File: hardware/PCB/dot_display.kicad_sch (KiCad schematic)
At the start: 33 parts, among them U10 MAX7219, U27 MAX7219, U29 MAX7219, U3 MAX7219, U31 MAX7219, U4 MAX7219, U6 MAX7219, U7 MAX7219

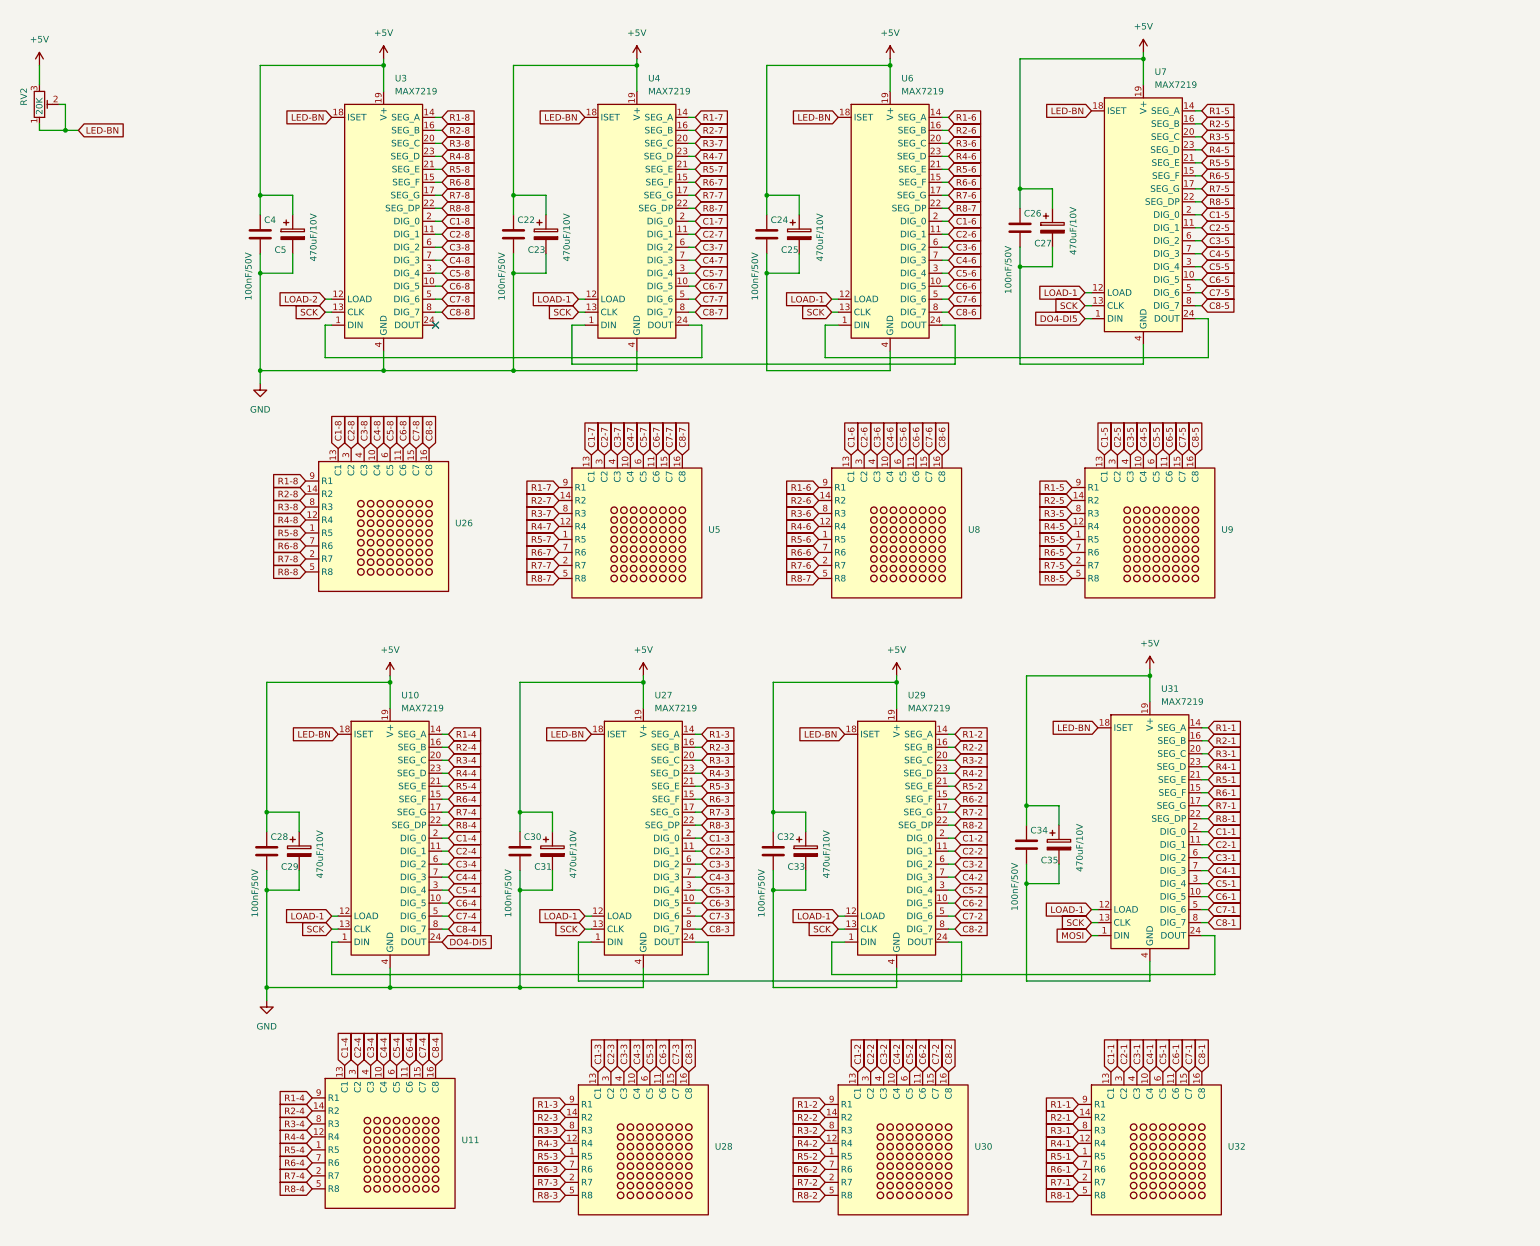
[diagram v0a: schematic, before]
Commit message: added KiCad libraries schematic bugfixes
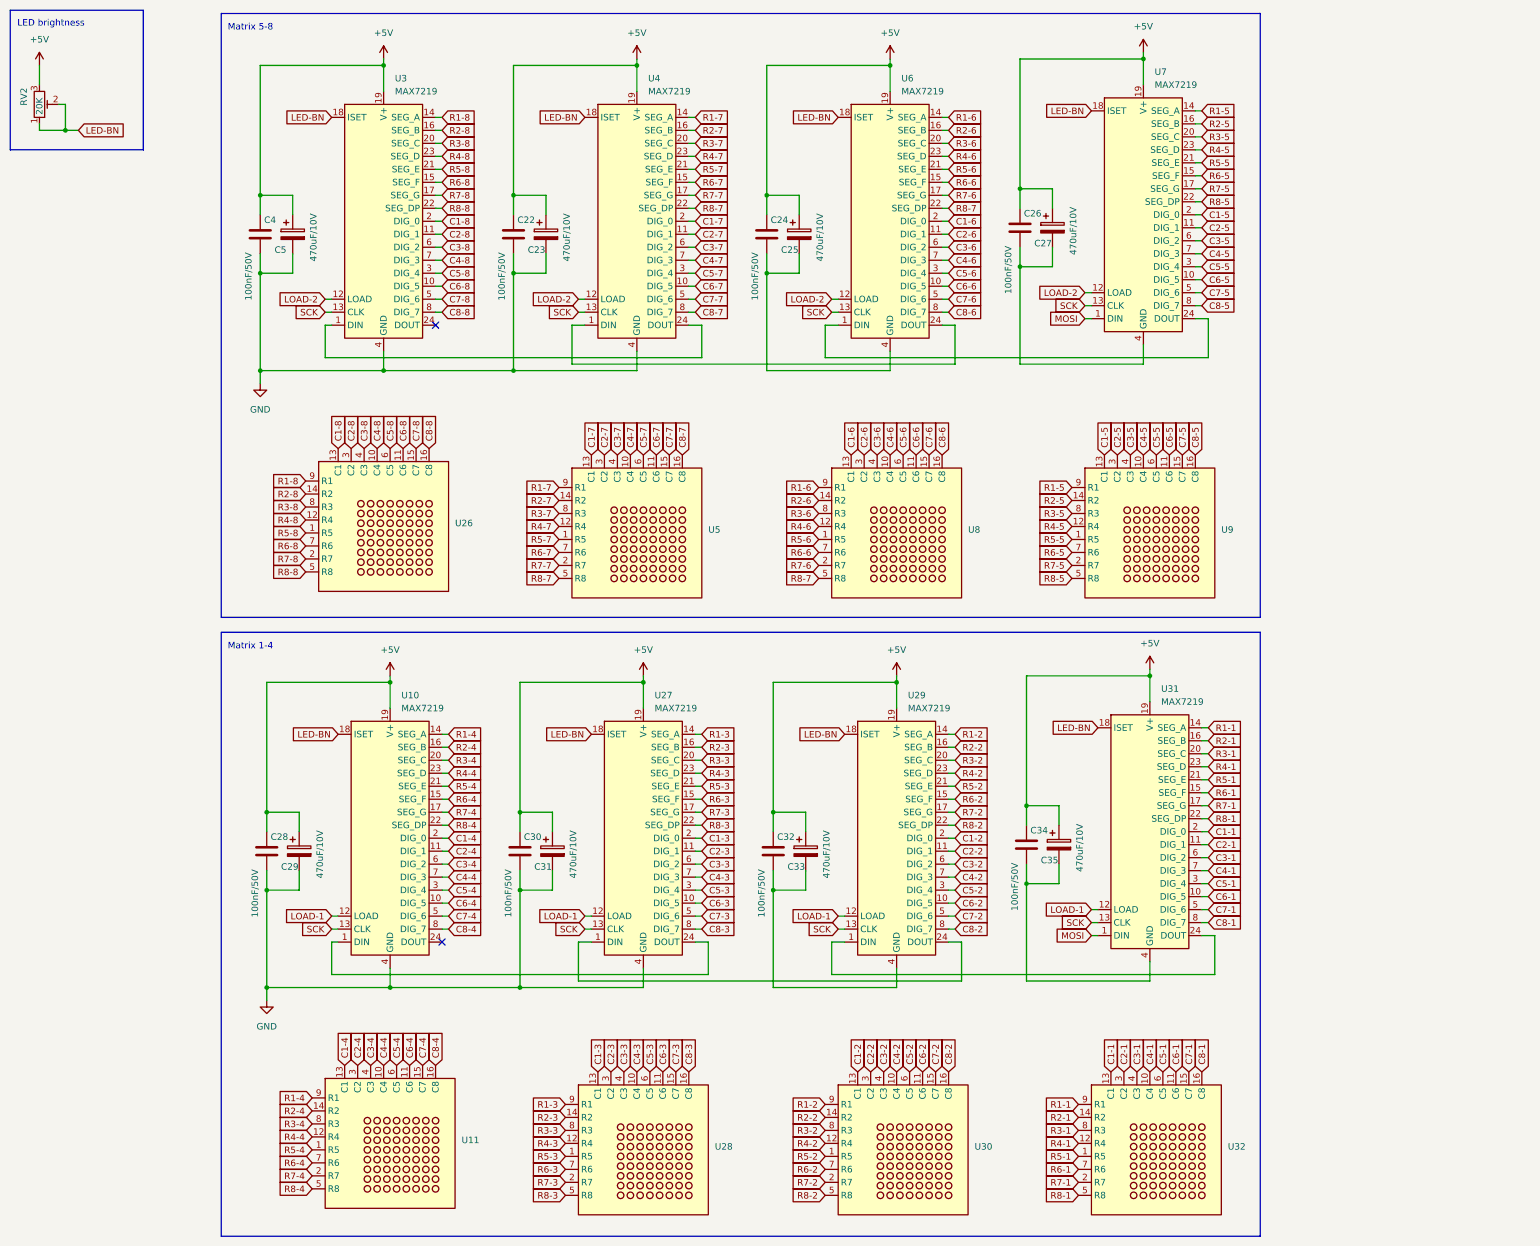
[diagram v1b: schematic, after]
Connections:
- net LOAD-1: no longer U4.12 (LOAD), U6.12 (LOAD), U7.12 (LOAD)
- net LOAD-2: now also U4.12 (LOAD), U6.12 (LOAD), U7.12 (LOAD)
- net MOSI: now also U7.1 (DIN)
- net DO4-DI5: no longer names the net of U10.24 (DOUT)
- net DO4-DI5: no longer U7.1 (DIN)
- no-connect marks 1 -> 2
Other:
- note added: "LED brightness"
- note added: "Matrix 1-4"
- note added: "Matrix 5-8"
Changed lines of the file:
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@@
 	)
 	(no_connect
+		(at 118.11 207.01)
+	)
+	(no_connect
 		(at 116.84 86.36)
 	)
@@
 		)
 	)
+	(rectangle
+		(start 74.93 146.431)
+		(end 278.13 264.541)
+		(stroke
+			(width 0)
+			(type default)
+		)
+		(fill
+			(type none)
+		)
+	)
+	(rectangle
+		(start 74.93 25.4)
+		(end 278.13 143.51)
+		(stroke
+			(width 0)
+			(type default)
+		)
+		(fill
+			(type none)
+		)
+	)
+	(rectangle
+		(start 33.655 24.765)
+		(end 59.69 52.07)
+		(stroke
+			(width 0)
+			(type default)
+		)
+		(fill
+			(type none)
+		)
+	)
+	(text "LED brightness"
+		(exclude_from_sim no)
+		(at 35.052 27.432 0)
+		(effects
+			(font
+				(size 1.27 1.27)
+			)
+			(justify left)
+		)
+	)
+	(text "Matrix 5-8"
+		(exclude_from_sim no)
+		(at 76.2 28.194 0)
+		(effects
+			(font
+				(size 1.27 1.27)
+			)
+			(justify left)
+		)
+	)
+	(text "Matrix 1-4"
+		(exclude_from_sim no)
+		(at 76.2 149.225 0)
+		(effects
+			(font
+				(size 1.27 1.27)
+			)
+			(justify left)
+		)
+	)
 	(global_label "C7-4"
 		(shape input)
@@
 		)
 	)
-	(global_label "DO4-DI5"
+	(global_label "MOSI"
 		(shape input)
 		(at 243.84 85.09 180)
@@
 		)
 		(property "Intersheetrefs" "${INTERSHEET_REFS}"
-			(at 232.3881 85.09 0)
+			(at 236.2586 85.09 0)
 			(effects
 				(font
@@
 		)
 	)
-	(global_label "LOAD-1"
+	(global_label "LOAD-2"
 		(shape input)
 		(at 243.84 80.01 180)
@@
 		)
 	)
-	(global_label "LOAD-1"
+	(global_label "LOAD-2"
 		(shape input)
 		(at 194.31 81.28 180)
@@
 		)
 	)
-	(global_label "LOAD-1"
+	(global_label "LOAD-2"
 		(shape input)
 		(at 144.78 81.28 180)
@@
 				(hide yes)
 			)
-		)
-	)
-	(global_label "DO4-DI5"
-		(shape input)
-		(at 118.11 207.01 0)
-		(fields_autoplaced yes)
-		(effects
-			(font
-				(size 1.27 1.27)
-			)
-			(justify left)
-		)
-		(property "Intersheetrefs" "${INTERSHEET_REFS}"
-			(at 129.5619 207.01 0)
-			(effects
-				(font
-					(size 1.27 1.27)
-				)
-				(justify left)
-				(hide yes)
-			)

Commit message: new harware bugfixes while building the prototype
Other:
- title: Dot Matrix Display -> DigiSlate+
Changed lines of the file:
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@@
 	(paper "A3")
 	(title_block
-		(title "Dot Matrix Display")
-		(date "2024-09-11")
-		(rev "1.0")
+		(title "DigiSlate+")
+		(date "2024-09-05")
+		(rev "1.1")
 	)
 	(junction

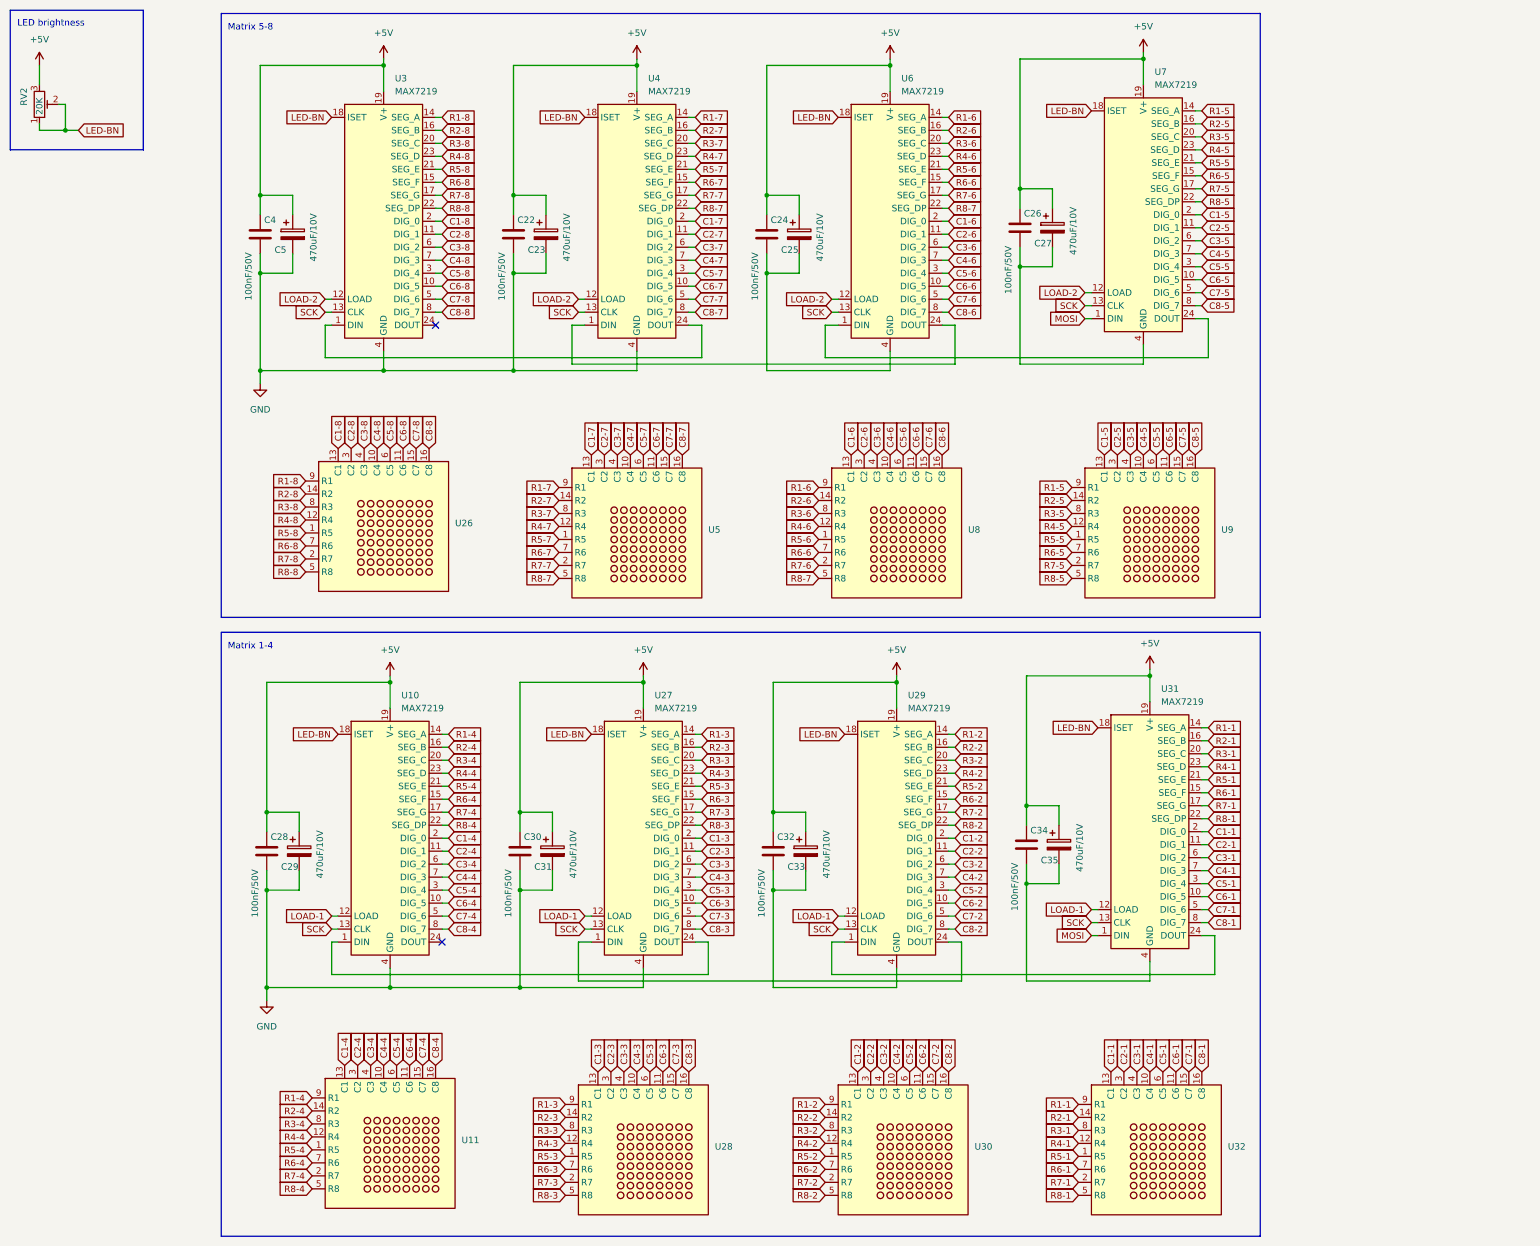
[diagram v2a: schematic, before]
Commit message: level converter added to schematic and pcb
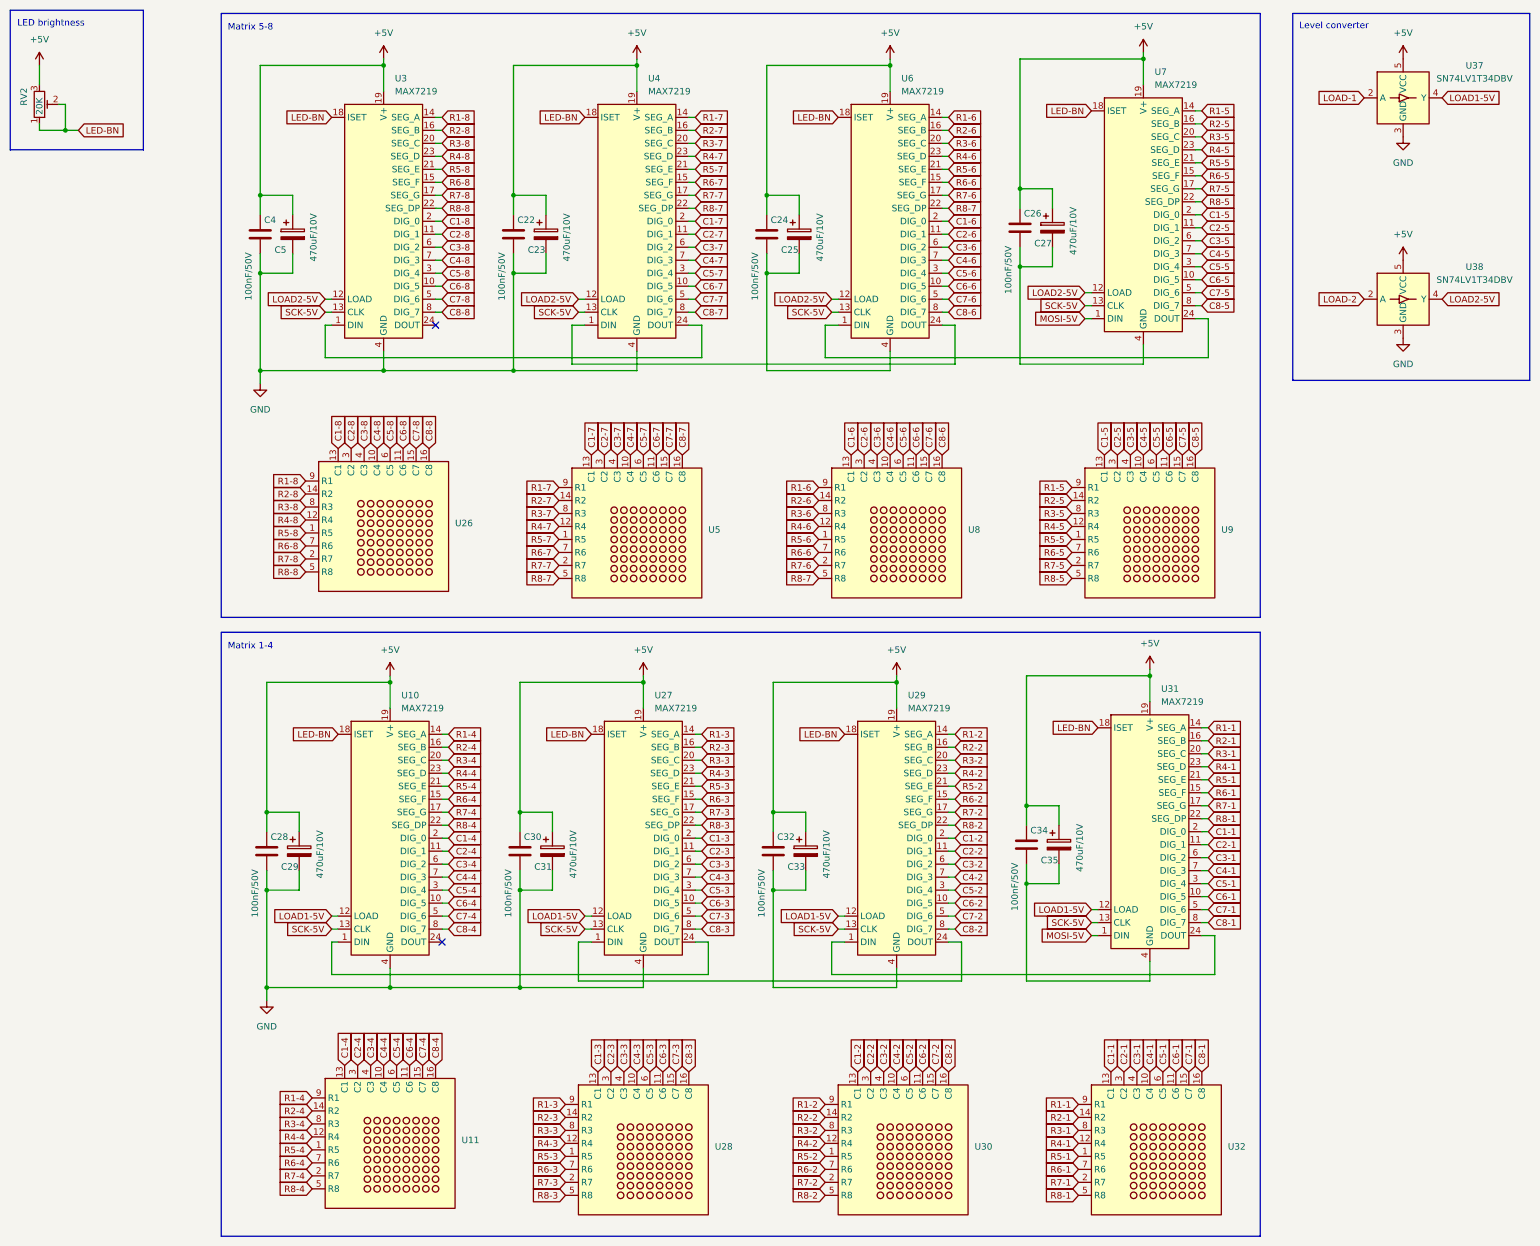
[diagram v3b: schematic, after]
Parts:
- added U37, U38: SN74LV1T34DBV, Package_TO_SOT_SMD:SOT-23-5, symbol Logic_LevelTranslator:SN74LV1T34DBV
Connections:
- net +5V: now also U37.5 (VCC), U38.5 (VCC)
- net GND: now also U37.3 (GND), U38.3 (GND)
- net LOAD-1: now also U37.2 (A); no longer U10.12 (LOAD), U27.12 (LOAD), U29.12 (LOAD), U31.12 (LOAD)
- net LOAD-2: now also U38.2 (A); no longer U3.12 (LOAD), U4.12 (LOAD), U6.12 (LOAD), U7.12 (LOAD)
- net MOSI renamed MOSI-5V
- net SCK renamed SCK-5V
- new net LOAD1-5V: U10.12 (LOAD), U27.12 (LOAD), U29.12 (LOAD), U31.12 (LOAD), U37.4 (Y)
- new net LOAD2-5V: U3.12 (LOAD), U38.4 (Y), U4.12 (LOAD), U6.12 (LOAD), U7.12 (LOAD)
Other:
- note added: "Level converter"
